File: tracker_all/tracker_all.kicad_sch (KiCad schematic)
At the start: 1 part, among them J1 GPS_MOUDLE_WITH_COMPASS

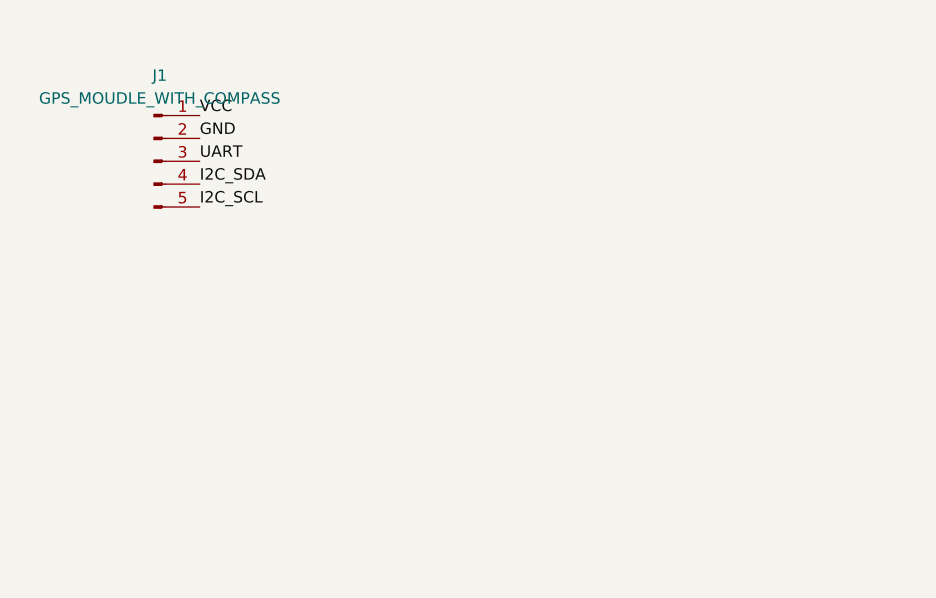
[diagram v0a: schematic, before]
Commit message: updated with all the components in the schematic
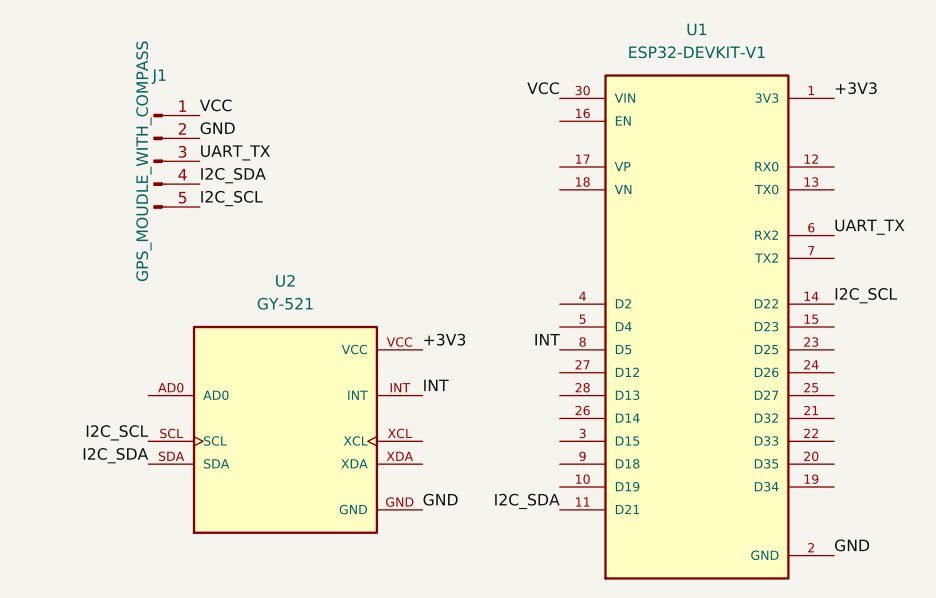
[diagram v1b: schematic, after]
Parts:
- added U1: ESP32-DEVKIT-V1, ESP32-DEVKIT-V1:MODULE_ESP32_DEVKIT_V1, symbol ESP32-DEVKIT-V1:ESP32-DEVKIT-V1
- added U2: GY-521, GY-521:MODULE_GY-521, symbol GY-521:GY-521
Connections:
- net GND: now also U1.2 (GND), U1.29 (GND), U2.GND
- net I2C_SCL: now also U1.14 (D22), U2.SCL
- net I2C_SDA: now also U1.11 (D21), U2.SDA
- net VCC: now also U1.30 (VIN)
- net UART renamed UART_TX
- net UART_TX: now also U1.6 (RX2)
- new net +3V3: U1.1 (3V3), U2.VCC
- new net INT: U1.8 (D5), U2.INT
